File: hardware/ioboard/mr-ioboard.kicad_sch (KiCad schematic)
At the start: 108 parts

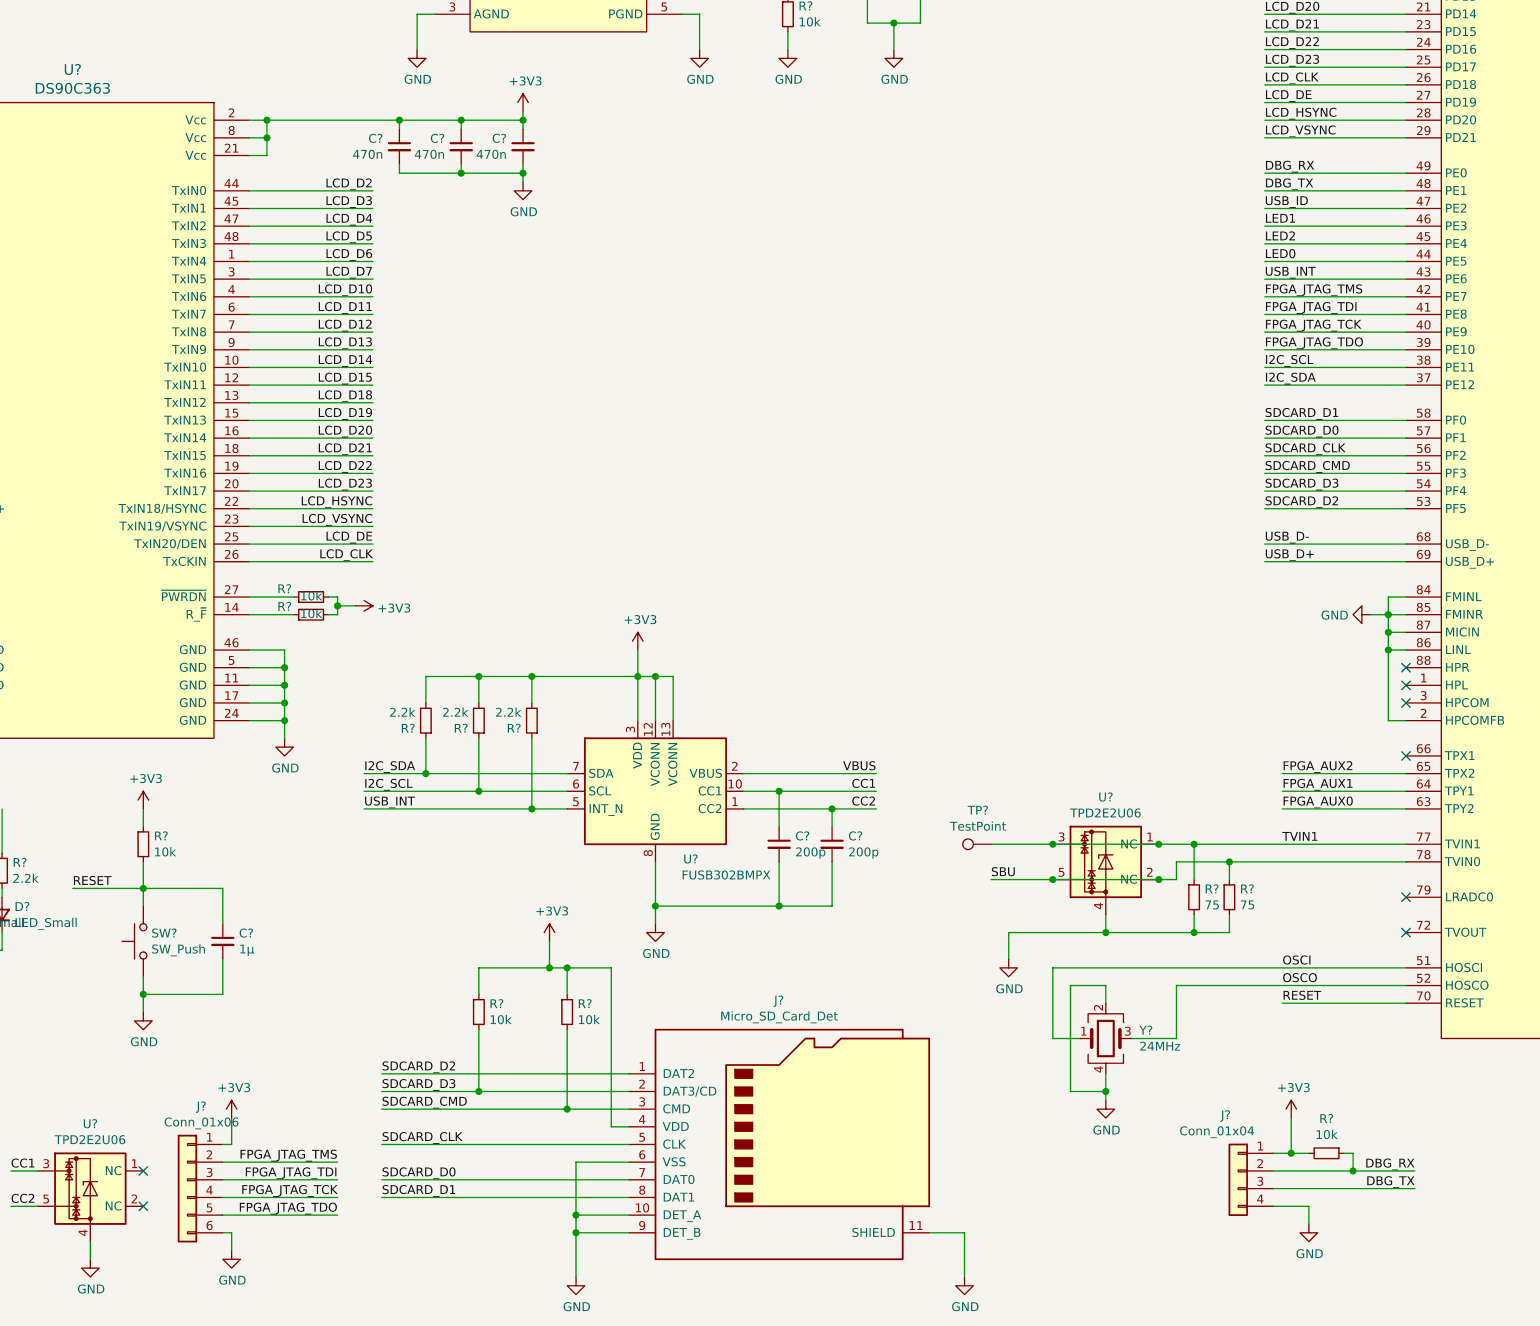
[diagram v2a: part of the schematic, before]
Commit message: Add WiFi module to IO board
Signed-off-by: gatecat <gatecat@ds0.me>
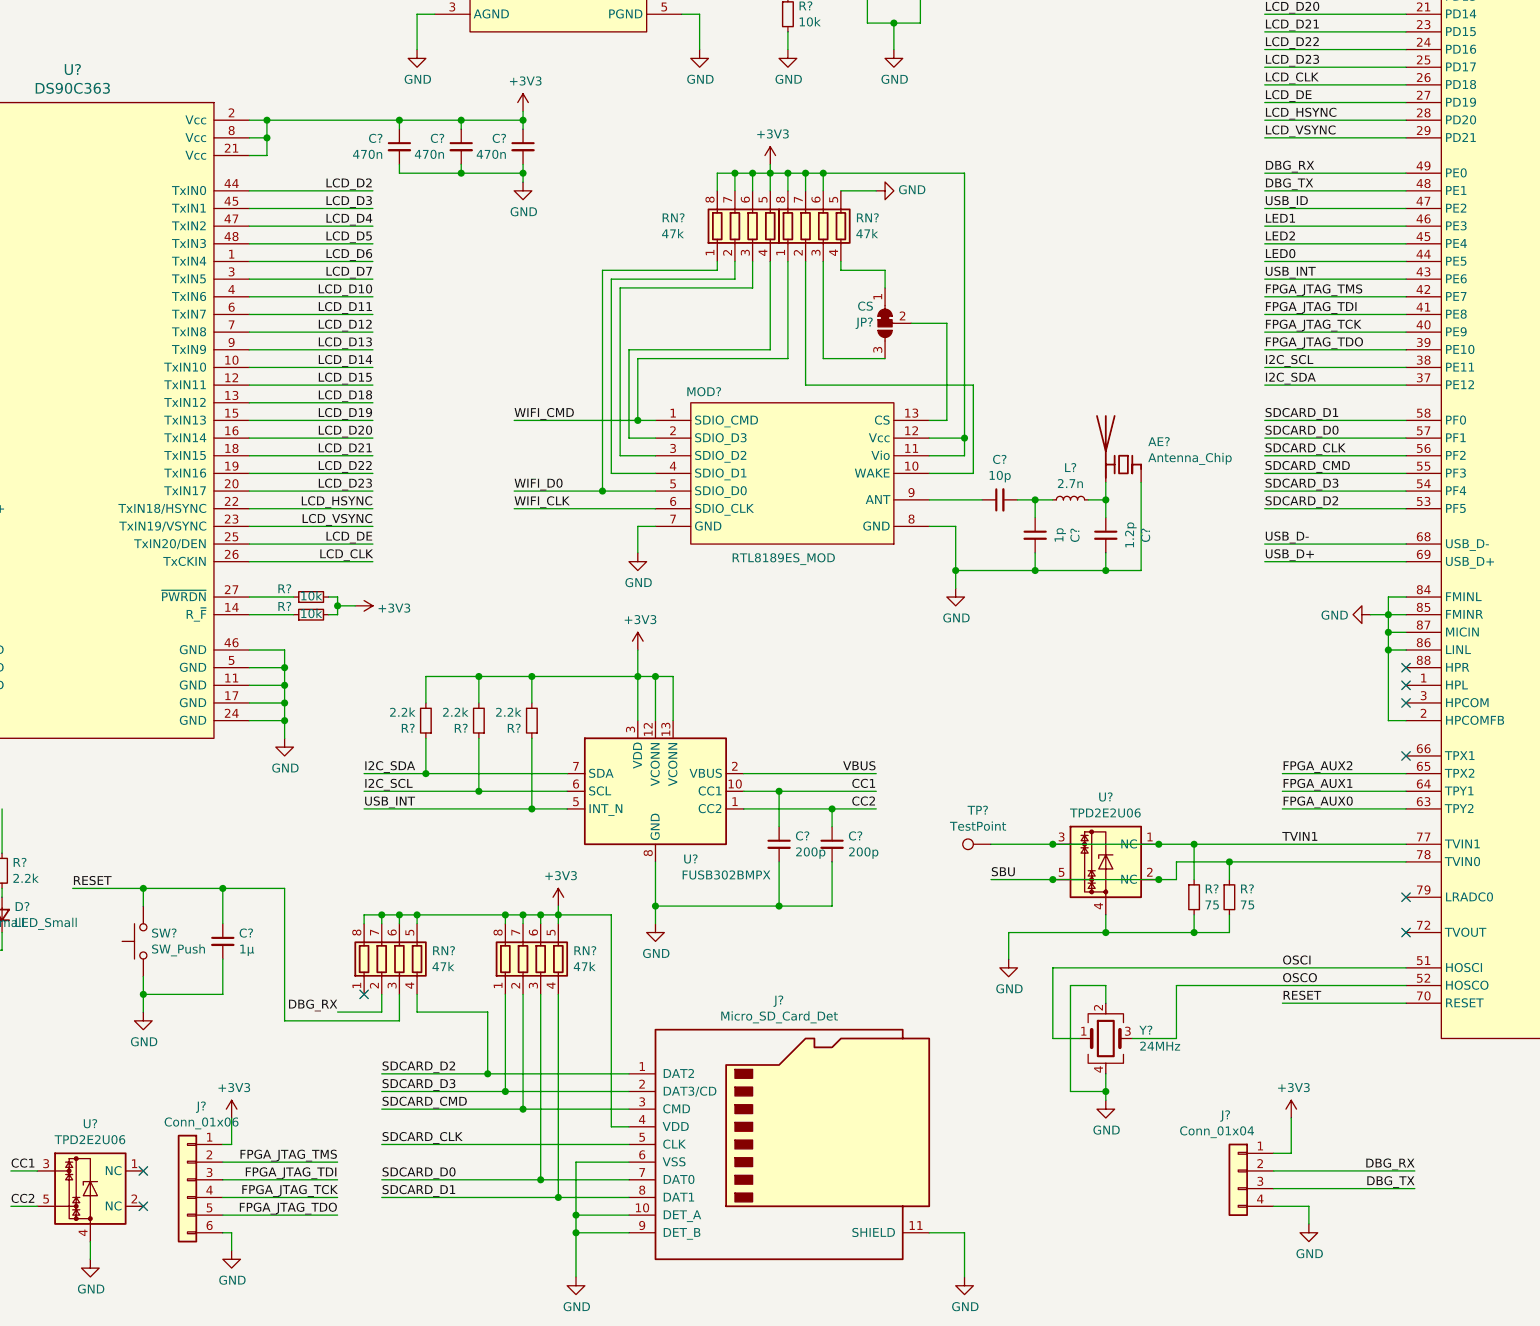
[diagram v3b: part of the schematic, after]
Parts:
- removed R? (x4): 10k, symbol Device:R_Small
- added AE?: Antenna_Chip, symbol Device:Antenna_Chip
- added C?: 1p, symbol Device:C_Small
- added C?: 10p, symbol Device:C_Small
- added C?: 1.2p, symbol Device:C_Small
- added JP?: CS, symbol Jumper:SolderJumper_3_Bridged12
- added L?: 2.7n, symbol Device:L_Small
- added MOD?: RTL8189ES_MOD, symbol meowality:RTL8189ES_MOD
- added RN? (x4): 47k, symbol Device:R_Pack04
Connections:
- net +3V3: now also MOD?.11 (Vio), MOD?.12 (Vcc), RN?.5 (R4.2), RN?.5 (R4.2), RN?.5 (R4.2), RN?.6 (R3.2), RN?.6 (R3.2), RN?.6 (R3.2), RN?.6 (R3.2), RN?.7 (R2.2), RN?.7 (R2.2), RN?.7 (R2.2), RN?.7 (R2.2), RN?.8 (R1.2), RN?.8 (R1.2), RN?.8 (R1.2), RN?.8 (R1.2)
- net DBG_RX: now also RN?.2 (R2.1)
- net GND: now also AE?.1 (FEED), C?.2, C?.2, MOD?.7 (GND), MOD?.8 (GND), RN?.5 (R4.2)
- net RESET: now also RN?.3 (R3.1)
- net SDCARD_CMD: now also RN?.2 (R2.1)
- net SDCARD_D0: now also RN?.3 (R3.1)
- net SDCARD_D1: now also RN?.4 (R4.1)
- net SDCARD_D2: now also RN?.4 (R4.1)
- net SDCARD_D3: now also RN?.1 (R1.1)
- net WIFI_CLK: now also MOD?.6 (SDIO_CLK)
- net WIFI_CMD: now also MOD?.1 (SDIO_CMD), RN?.1 (R1.1)
- net WIFI_D0: now also MOD?.5 (SDIO_D0), RN?.1 (R1.1)
- new net: MOD?.10 (WAKE), RN?.2 (R2.1)
- new net: JP?.3 (B), RN?.3 (R3.1)
- new net: JP?.1 (A), RN?.4 (R4.1)
- new net: C?.1, C?.2, L?.1
- new net: C?.1, MOD?.9 (ANT)
- new net: AE?.2 (PCB_Trace), C?.1, L?.2
- new net: JP?.2 (C), MOD?.13 (CS)
- new net: MOD?.4 (SDIO_D1), RN?.2 (R2.1)
- new net: MOD?.3 (SDIO_D2), RN?.3 (R3.1)
- new net: MOD?.2 (SDIO_D3), RN?.4 (R4.1)
- no-connect marks 20 -> 21

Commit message: Assign some footprints & fix values for IO board
Signed-off-by: gatecat <gatecat@ds0.me>
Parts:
- AE1: renamed from AE?; footprint (none) -> RF_Antenna:Johanson_2450AT43F0100
- C11: renamed from C?; value NC -> 100p; footprint (none) -> Capacitor_SMD:C_0402_1005Metric
- C12, C48, C49, C50: renamed from C?; footprint (none) -> Capacitor_SMD:C_0603_1608Metric
- C14, C16, C17, C2, C30, C31, C32, C4, C44, C46, C47, C51: renamed from C?; footprint (none) -> Capacitor_SMD:C_0805_2012Metric
- C18, C19, C20, C23, C24, C27, C28, C29, C33, C34, C35, C36, C37, C38, C39, C40, C41, C42, C43, C45, C6, C7, C9: renamed from C?; footprint (none) -> Capacitor_SMD:C_0402_1005Metric
- C5: renamed from C?; footprint (none) -> Capacitor_Tantalum_SMD:CP_EIA-3528-12_Kemet-T
- D1, D2, D3, D4: renamed from D?; footprint (none) -> LED_SMD:LED_0805_2012Metric
- FB1: renamed from FB?; footprint (none) -> Inductor_SMD:L_0603_1608Metric
- J2: renamed from J?; footprint (none) -> Connector_USB:USB_C_Receptacle_GCT_USB4085
- J3: renamed from J?; footprint (none) -> Connector_PinHeader_2.54mm:PinHeader_1x06_P2.54mm_Vertical
- J5: renamed from J?; footprint (none) -> Connector_PinHeader_2.54mm:PinHeader_1x04_P2.54mm_Vertical
- JP1: renamed from JP?; footprint (none) -> Jumper:SolderJumper-3_P1.3mm_Bridged12_Pad1.0x1.5mm
- L2: renamed from L?; value 3.3u -> 2.2u; footprint (none) -> Inductor_SMD:L_Bourns_SRP7028A_7.3x6.6mm
- L4: renamed from L?; footprint (none) -> Inductor_SMD:L_0402_1005Metric
- R10, R11, R12, R13, R14, R16, R17, R18, R2, R21, R22, R23, R24, R25, R26, R27, R28, R3, R4, R7, R8: renamed from R?; footprint (none) -> Resistor_SMD:R_0402_1005Metric
- R9: renamed from R?; value NC -> 20k; footprint (none) -> Resistor_SMD:R_0402_1005Metric
- RN1, RN2, RN3, RN4: renamed from RN?; footprint (none) -> Resistor_SMD:R_0402_1005Metric
- SW1: renamed from SW?; footprint (none) -> Button_Switch_SMD:SW_SPST_B3U-1000P
- TP1, TP2: renamed from TP?; footprint (none) -> TestPoint:TestPoint_Pad_D2.0mm
- U4: renamed from U?; footprint (none) -> Package_SO:TSSOP-48_8x12.5mm_P0.5mm
- Y1: renamed from Y?; footprint (none) -> Oscillator:Oscillator_SMD_EuroQuartz_XO32-4Pin_3.2x2.5mm
- gave numbers to parts that had none: 31

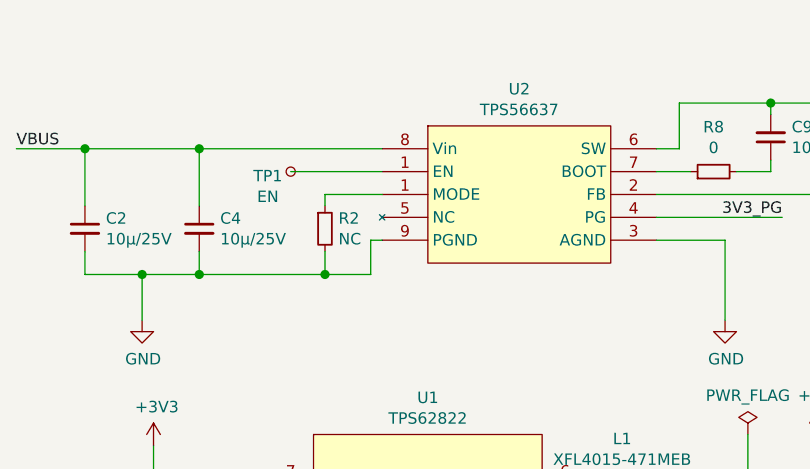
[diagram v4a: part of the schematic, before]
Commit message: Create some footprints for the IO board
Signed-off-by: gatecat <gatecat@ds0.me>
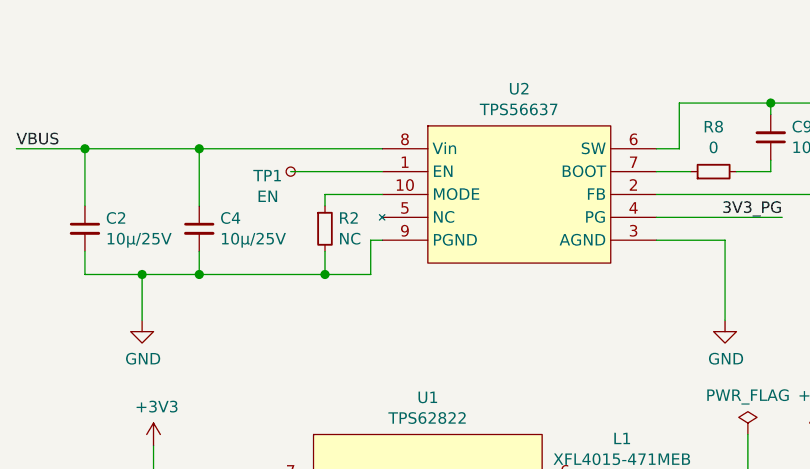
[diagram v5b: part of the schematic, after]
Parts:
- MOD1: footprint (none) -> meowality:RTL8189ES_MOD
- U10: footprint (none) -> meowality:QFN-88_EP_10x10_Pitch0.4mm
- U2: footprint (none) -> meowality:VQFN10-HR
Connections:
- net at R2.1: now also U2.10 (MODE); no longer U2.1 (MODE)
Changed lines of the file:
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@@
     (property "Reference" "U2" (id 0) (at 73.66 22.5863 0))
     (property "Value" "TPS56637" (id 1) (at 73.66 24.885 0))
-    (property "Footprint" "" (id 2) (at 73.66 34.29 0)
+    (property "Footprint" "meowality:VQFN10-HR" (id 2) (at 73.66 34.29 0)
       (effects (font (size 1.27 1.27)) hide)
     )
@@
     (pin "8")
     (pin "1")
-    (pin "1")
+    (pin "10")
     (pin "5")
     (pin "9")
@@
     (property "Reference" "MOD1" (id 0) (at 193.675 152.1263 0))
     (property "Value" "RTL8189ES_MOD" (id 1) (at 205.105 176.015 0))
-    (property "Footprint" "" (id 2) (at 205.74 163.83 0)
+    (property "Footprint" "meowality:RTL8189ES_MOD" (id 2) (at 205.74 163.83 0)
       (effects (font (size 1.27 1.27)) hide)
     )
@@
     (property "Reference" "U10" (id 0) (at 320.04 42.9063 0))
     (property "Value" "F1C200S" (id 1) (at 320.04 45.205 0))
-    (property "Footprint" "" (id 2) (at 320.04 245.11 0)
+    (property "Footprint" "meowality:QFN-88_EP_10x10_Pitch0.4mm" (id 2) (at 320.04 245.11 0)
       (effects (font (size 1.27 1.27)) hide)
     )
@@
     )
     (path "/bf767ab0-d986-441b-9076-8f9d5f44d287"
-      (reference "MOD1") (unit 1) (value "RTL8189ES_MOD") (footprint "")
+      (reference "MOD1") (unit 1) (value "RTL8189ES_MOD") (footprint "meowality:RTL8189ES_MOD")
     )
     (path "/ba7dc5a4-c446-4388-bb83-ffa143516649"
@@
     )
     (path "/b6581bf3-66aa-460d-9329-57bba0dead5f"
-      (reference "U2") (unit 1) (value "TPS56637") (footprint "")
+      (reference "U2") (unit 1) (value "TPS56637") (footprint "meowality:VQFN10-HR")
     )
     (path "/53d12aea-c49c-4c1b-b028-be0c53dc30ce"
@@
     )
     (path "/86a39066-7989-449a-90f9-ad2b9221de0b"
-      (reference "U10") (unit 1) (value "F1C200S") (footprint "")
+      (reference "U10") (unit 1) (value "F1C200S") (footprint "meowality:QFN-88_EP_10x10_Pitch0.4mm")
     )
     (path "/2e10c69a-17b4-427c-803a-af2b102c7a30"
